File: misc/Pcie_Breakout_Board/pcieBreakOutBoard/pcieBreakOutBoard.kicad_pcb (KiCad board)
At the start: 2 copper layers, 53 x 45.2 mm, 1 part, among them J1 2041119-1 (Mini Pcie Express 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

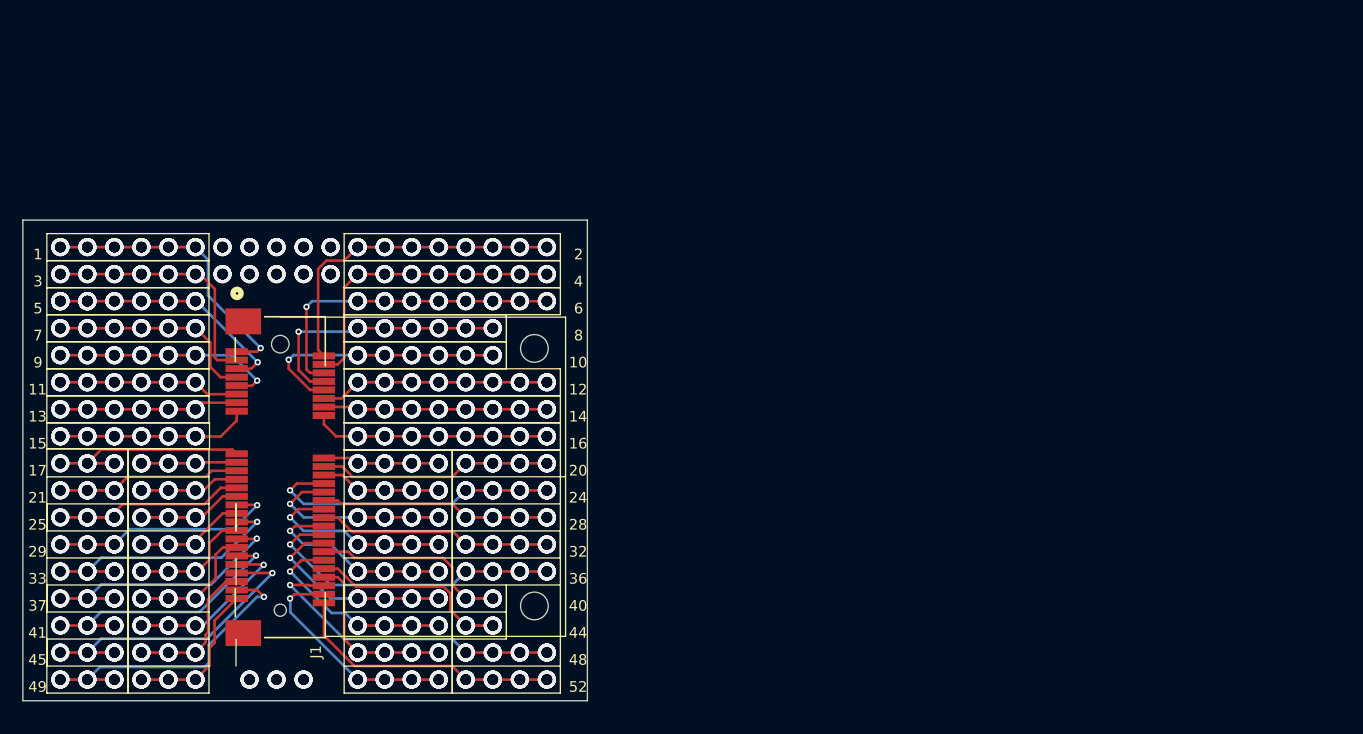
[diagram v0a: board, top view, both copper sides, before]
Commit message: routing
Start routing of the jtag part
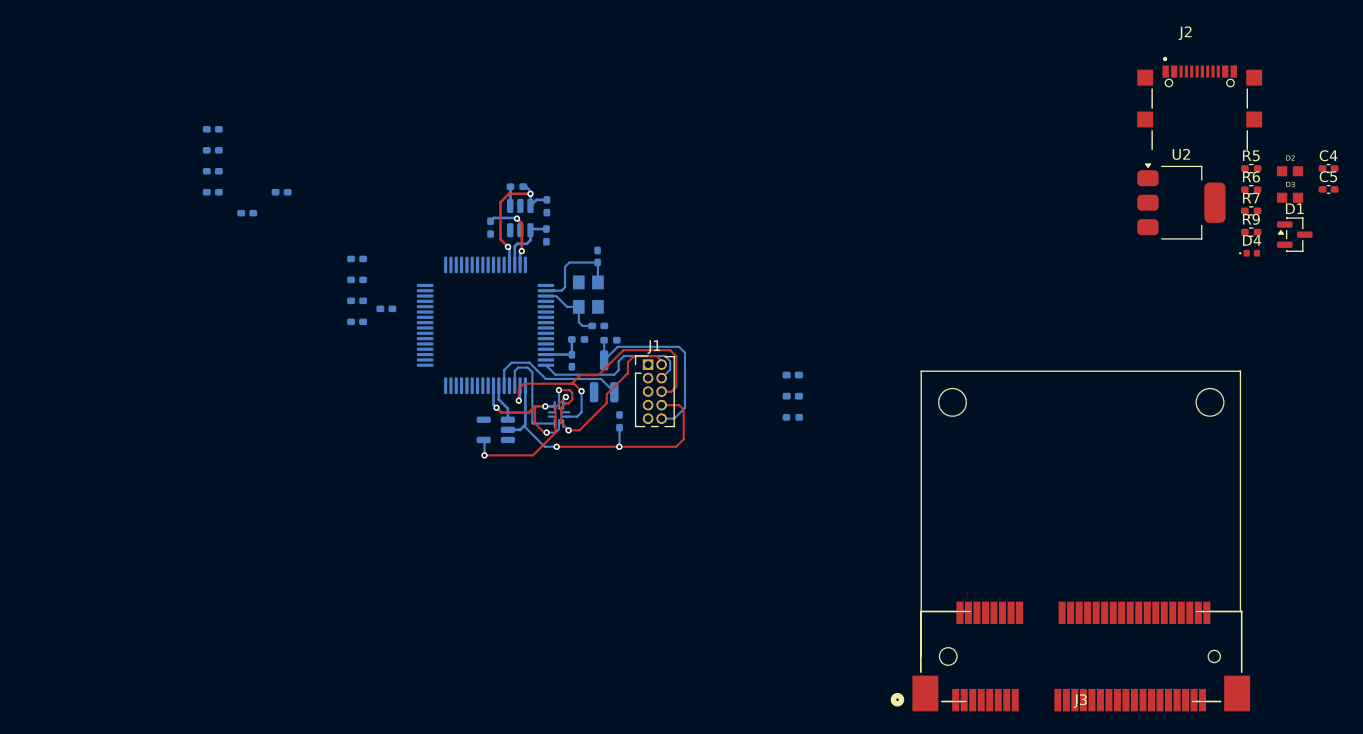
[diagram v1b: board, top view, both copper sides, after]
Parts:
- added C1: 27pF, Capacitor_SMD:C_0402_1005Metric_Pad0.74x0.62mm_HandSolder, B.Cu at (169.9, 81.1)
- added C10: 100nF, Capacitor_SMD:C_0402_1005Metric_Pad0.74x0.62mm_HandSolder, B.Cu at (147.3, 78.7)
- added C11: 3.3uF, Capacitor_SMD:C_0402_1005Metric_Pad0.74x0.62mm_HandSolder, B.Cu at (147.3, 80.7)
- added C12: 100nF, Capacitor_SMD:C_0402_1005Metric_Pad0.74x0.62mm_HandSolder, B.Cu at (136.9, 70.5)
- added C13: 100nF, Capacitor_SMD:C_0402_1005Metric_Pad0.74x0.62mm_HandSolder, B.Cu at (133.7, 62.6)
- added C15: 100nF, Capacitor_SMD:C_0402_1005Metric_Pad0.74x0.62mm_HandSolder, B.Cu at (133.7, 64.6)
- added C16: 100nF, Capacitor_SMD:C_0402_1005Metric_Pad0.74x0.62mm_HandSolder, B.Cu at (133.7, 66.5)
- added C17: 100nF, Capacitor_SMD:C_0402_1005Metric_Pad0.74x0.62mm_HandSolder, B.Cu at (133.7, 68.5)
- added C2: 10nF, Capacitor_SMD:C_0402_1005Metric_Pad0.74x0.62mm_HandSolder, B.Cu at (167.4, 84.3)
- added C3: 27pF, Capacitor_SMD:C_0402_1005Metric_Pad0.74x0.62mm_HandSolder, B.Cu at (169.9, 74.5)
- added C4: 1uF, Capacitor_SMD:C_0402_1005Metric_Pad0.74x0.62mm_HandSolder, F.Cu at (238.6, 66.3)
- added C5: 4.7uF, Capacitor_SMD:C_0402_1005Metric_Pad0.74x0.62mm_HandSolder, F.Cu at (238.6, 68.2)
- added C6: 100nF, Capacitor_SMD:C_0402_1005Metric_Pad0.74x0.62mm_HandSolder, B.Cu at (140.2, 68.5)
- added C7: 100nF, Capacitor_SMD:C_0402_1005Metric_Pad0.74x0.62mm_HandSolder, B.Cu at (150.0, 79.5)
- added C8: 4.1uF, Capacitor_SMD:C_0402_1005Metric_Pad0.74x0.62mm_HandSolder, B.Cu at (147.3, 74.8)
- added C9: 4.1uF, Capacitor_SMD:C_0402_1005Metric_Pad0.74x0.62mm_HandSolder, B.Cu at (147.3, 76.7)
- added D1: BAT54C, Package_TO_SOT_SMD:SOT-23, F.Cu at (235.4, 72.5)
- added D2: PGB1010603NR, User_Footprint:DIOC1608X36N, F.Cu at (234.9, 66.5)
- added D3: PGB1010603NR, User_Footprint:DIOC1608X36N, F.Cu at (234.9, 69.0)
- added D4: LED, LED_SMD:LED_0402_1005Metric, F.Cu at (231.3, 74.2)
- added J2: USB_C_Receptacle_USB2.0_16P, User_Footprint:AMPHENOL_GSB1C41110SSHR, F.Cu at (226.5, 60.8)
- added J3: 2041119-1 (Mini Pcie Express Half), User_Footprint:CONN_2041119-1_TEC, F.Cu at (215.3, 112.1)
- added L1: L, Inductor_SMD:L_0402_1005Metric_Pad0.77x0.64mm_HandSolder, B.Cu at (188.2, 85.7)
- added L2: L, Inductor_SMD:L_0402_1005Metric_Pad0.77x0.64mm_HandSolder, B.Cu at (188.2, 87.7)
- added Q1: MMBT2222A, Package_TO_SOT_SMD:SOT-23_Handsoldering, B.Cu at (170.5, 85.8)
- added R1: 12k, Resistor_SMD:R_0402_1005Metric_Pad0.72x0.64mm_HandSolder, B.Cu at (188.2, 89.7)
- added R10: 10k, Resistor_SMD:R_0402_1005Metric_Pad0.72x0.64mm_HandSolder, B.Cu at (165.1, 69.8)
- added R11: 10k, Resistor_SMD:R_0402_1005Metric_Pad0.72x0.64mm_HandSolder, B.Cu at (171.1, 82.4)
- added R12: 30K, Resistor_SMD:R_0402_1005Metric_Pad0.72x0.64mm_HandSolder, B.Cu at (171.9, 90.0)
- added R2: 10k, Resistor_SMD:R_0402_1005Metric_Pad0.72x0.64mm_HandSolder, B.Cu at (168.0, 82.3)
- added R3: 2k, Resistor_SMD:R_0402_1005Metric_Pad0.72x0.64mm_HandSolder, B.Cu at (162.3, 68.0)
- added R4: 10k, Resistor_SMD:R_0402_1005Metric_Pad0.72x0.64mm_HandSolder, B.Cu at (159.8, 71.8)
- added R5: 0, Resistor_SMD:R_0402_1005Metric_Pad0.72x0.64mm_HandSolder, F.Cu at (231.3, 66.3)
- added R6: 0, Resistor_SMD:R_0402_1005Metric_Pad0.72x0.64mm_HandSolder, F.Cu at (231.3, 68.3)
- added R7: 0, Resistor_SMD:R_0402_1005Metric_Pad0.72x0.64mm_HandSolder, F.Cu at (231.3, 70.3)
- added R8: 10k, Resistor_SMD:R_0402_1005Metric_Pad0.72x0.64mm_HandSolder, B.Cu at (165.1, 72.6)
- added R9: 100, Resistor_SMD:R_0402_1005Metric_Pad0.72x0.64mm_HandSolder, F.Cu at (231.3, 72.2)
- added U1: FT2232HL, Package_QFP:LQFP-64_10x10mm_P0.5mm, B.Cu at (159.3, 81.0)
- added U2: AP7361C-33E, Package_TO_SOT_SMD:SOT-223-3_TabPin2, F.Cu at (224.7, 69.5)
- added U3: 93LCxxBxxOT, Package_TO_SOT_SMD:SOT-23-6, B.Cu at (162.6, 70.9)
- added U4: NC7SZ125M5X, Package_TO_SOT_SMD:SOT-23-5, B.Cu at (160.3, 90.8)
- added U7: TS3A5223RSW, Package_DFN_QFN:Texas_RSW0010A_UQFN-10_1.4x1.8mm_P0.4mm, B.Cu at (166.2, 89.4)
- added Y1: ECS-120-20-33-AEL-TR, User_Footprint:XTAL_ECS-120-20-33-AEL-TR, B.Cu at (169.0, 78.1)
- J1: value 2041119-1 (Mini Pcie Express Half) -> Conn_ARM_JTAG_SWD_10; footprint User_Footprint:CONN_2041119-1_TEC -> Connector_PinHeader_1.27mm:PinHeader_2x05_P1.27mm_Vertical
- moved J1 36.1 mm to (174.6, 84.7), turned to 0 degrees
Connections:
- J1 pad 1: /Port1 -> +3V3
- J1 pad 10: /Port10 -> /Jtag/~{SRST}
- J1 pad 2: /Port2 -> /Jtag/TMS/SWDIO
- J1 pad 3: /Port3 -> GND
- J1 pad 4: /Port4 -> /Jtag/TCK/SWDCLK
- J1 pad 5: /Port5 -> GND
- J1 pad 6: /Port6 -> /Jtag/TDO
- J1 pad 7: /Port7 -> unconnected-(J1-KEY-Pad7)
- J1 pad 8: /Port8 -> /Jtag/TDI
- J1 pad 9: /Port9 -> GND
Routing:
- net /Port2: track 30.7 -> 0.00 mm, vias 24 -> 0
- net /Port6: track 30.5 -> 0.00 mm, vias 25 -> 0
- net /Port48: track 30.0 -> 0.00 mm, vias 13 -> 0
- net /Port36: track 29.8 -> 0.00 mm, vias 13 -> 0
- net /Port45: track 28.9 -> 0.00 mm, vias 9 -> 0
- net /Port49: track 28.7 -> 0.00 mm, vias 10 -> 0
- net /Port24: track 28.6 -> 0.00 mm, vias 13 -> 0
- net /Jtag/TDI: track 0.00 -> 28.5 mm, vias 0 -> 2
- net /Jtag/TDO: track 0.00 -> 28.4 mm, vias 0 -> 2
- net /Port4: track 28.3 -> 0.00 mm, vias 24 -> 0
- net /Port1: track 27.1 -> 0.00 mm, vias 19 -> 0
- net /Port52: track 25.7 -> 0.00 mm, vias 12 -> 0
- net /Port41: track 25.5 -> 0.00 mm, vias 9 -> 0
- net /Port37: track 25.3 -> 0.00 mm, vias 9 -> 0
- net /Port33: track 24.9 -> 0.00 mm, vias 9 -> 0
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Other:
- board size 53 x 45.2 mm -> 26.8 x 2.6 mm
- copper layers 2 -> 4
- board text removed: "1"
- board text removed: "10"
- board text removed: "11"
- board text removed: "12"
- board text removed: "13"
- board text removed: "14"
- board text removed: "15"
- board text removed: "16"
- board text removed: "17"
- board text removed: "18"
- board text removed: "19"
- board text removed: "2"
- board text removed: "20"
- board text removed: "21"
- board text removed: "22"
- board text removed: "23"
- board text removed: "24"
- board text removed: "25"
- board text removed: "26"
- board text removed: "27"
- board text removed: "28"
- board text removed: "29"
- board text removed: "3"
- board text removed: "30"
- board text removed: "31"
- board text removed: "32"
- board text removed: "33"
- board text removed: "34"
- board text removed: "35"
- board text removed: "36"
- board text removed: "37"
- board text removed: "38"
- board text removed: "39"
- board text removed: "4"
- board text removed: "40"
- board text removed: "41"
- board text removed: "42"
- board text removed: "43"
- board text removed: "44"
- board text removed: "45"
- board text removed: "46"
- board text removed: "47"
- board text removed: "48"
- board text removed: "49"
- board text removed: "5"
- board text removed: "50"
- board text removed: "51"
- board text removed: "52"
- board text removed: "6"
- board text removed: "7"
- board text removed: "8"
- board text removed: "9"

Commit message: layout
finished 70% of layout
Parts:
- added J4: Conn_02x04_Odd_Even, Connector_PinHeader_2.54mm:PinHeader_2x04_P2.54mm_Vertical, F.Cu at (136.6, 83.3)
- C13, C17, R1: moved to F.Cu
- C4, C5, D1, D2, D3, D4, R5, R6, R7, R9, U2: moved to B.Cu
- J3: footprint User_Footprint:CONN_2041119-1_TEC -> Connector_PCBEdge:BUS_PCI_Express_Mini_Half
- moved C4 108.8 mm to (130.3, 77.8), turned to 90 degrees
- moved C5 108.4 mm to (130.3, 74.2), turned to -90 degrees
- moved D1 107.6 mm to (127.8, 75.7), turned to -90 degrees
- moved D4 103.1 mm to (128.3, 70.7), turned to 180 degrees
- moved R9 102.9 mm to (128.4, 73.2)
- moved D3 102.7 mm to (132.3, 67.1), turned to 90 degrees
- moved R5 101.7 mm to (129.8, 72.2), turned to 180 degrees
- moved D2 100.5 mm to (134.4, 67.1), turned to -90 degrees
- moved R6 99.0 mm to (132.3, 70.8), turned to -90 degrees
- moved R7 97.0 mm to (134.3, 70.8), turned to -90 degrees
- moved J2 93.7 mm to (133.1, 68.6), turned to 180 degrees
- moved U2 89.2 mm to (135.8, 76.0)
- moved J3 60.8 mm to (155.9, 99.1)
- moved C13 35.0 mm to (162.3, 82.8)
- moved C15 34.0 mm to (158.0, 88.4)
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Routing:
- net /MiniPcieExHalf/Port8: track 0.00 -> 38.6 mm, vias 0 -> 3
- net /MiniPcieExHalf/Port4: track 0.00 -> 36.0 mm, vias 0 -> 2
- net /MiniPcieExHalf/Port12: track 0.00 -> 33.8 mm, vias 0 -> 3
- net /MiniPcieExHalf/Port18: track 0.00 -> 33.1 mm, vias 0 -> 1
- net /MiniPcieExHalf/Port6: track 0.00 -> 32.3 mm, vias 0 -> 3
- net /MiniPcieExHalf/Port20: track 0.00 -> 31.7 mm, vias 0 -> 1
- net /MiniPcieExHalf/Port16: track 0.00 -> 31.7 mm, vias 0 -> 3
- net /MiniPcieExHalf/Port2: track 0.00 -> 30.5 mm, vias 0 -> 2
- net /MiniPcieExHalf/Port22: track 0.00 -> 29.4 mm, vias 0 -> 1
- net /Jtag/~{DCD}: track 0.00 -> 27.8 mm, vias 0 -> 1
- net /MiniPcieExHalf/Port10: track 0.00 -> 27.3 mm, vias 0 -> 2
- net /MiniPcieExHalf/Port14: track 0.00 -> 26.7 mm, vias 0 -> 3
- net /Jtag/~{DSR}: track 0.00 -> 24.6 mm, vias 0 -> 1
- net /Jtag/TXD: track 0.00 -> 23.4 mm, vias 0 -> 1
- net /Jtag/RXD: track 0.00 -> 21.9 mm, vias 0 -> 1
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- added copper zone on In2.Cu, net +3V3
- added copper zone on In1.Cu, net GND
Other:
- board size 26.8 x 2.6 mm -> 54 x 50.8 mm

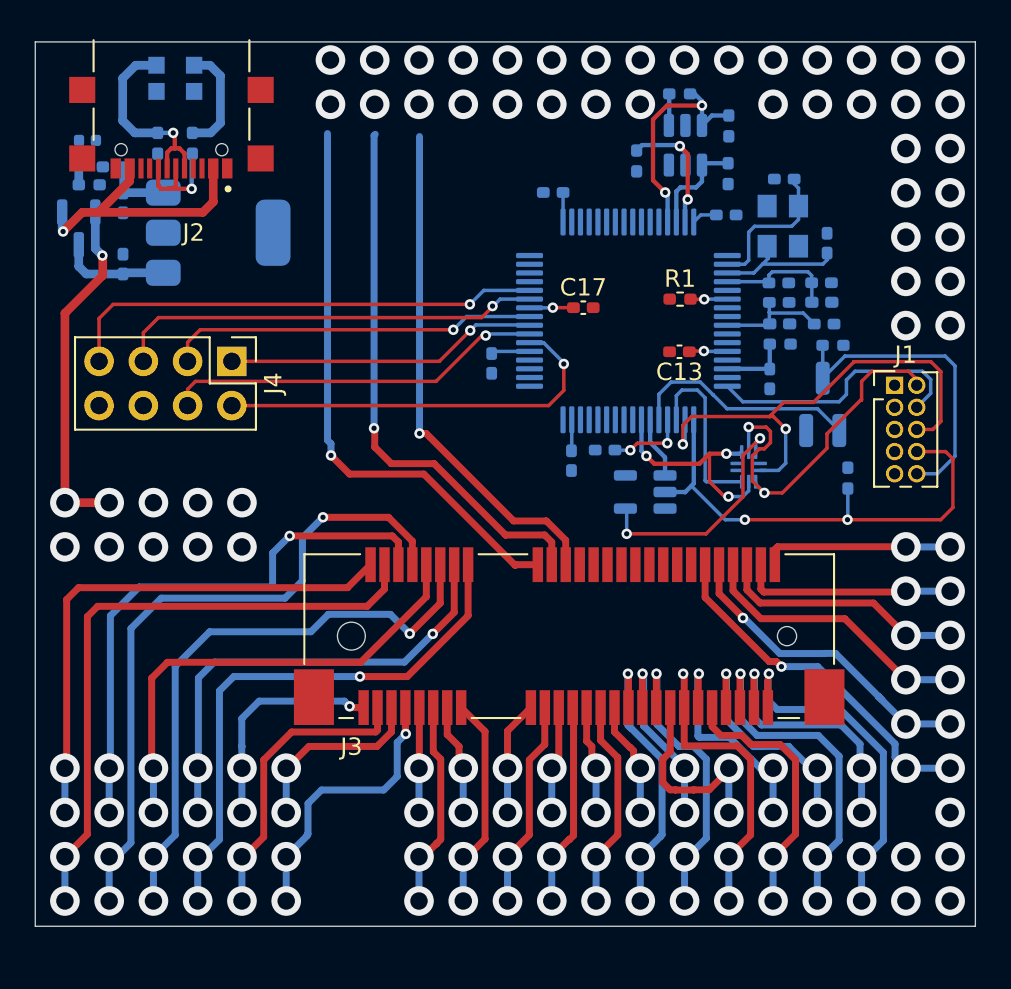
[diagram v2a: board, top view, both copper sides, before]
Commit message: Routing
Finish layout needs to be checked
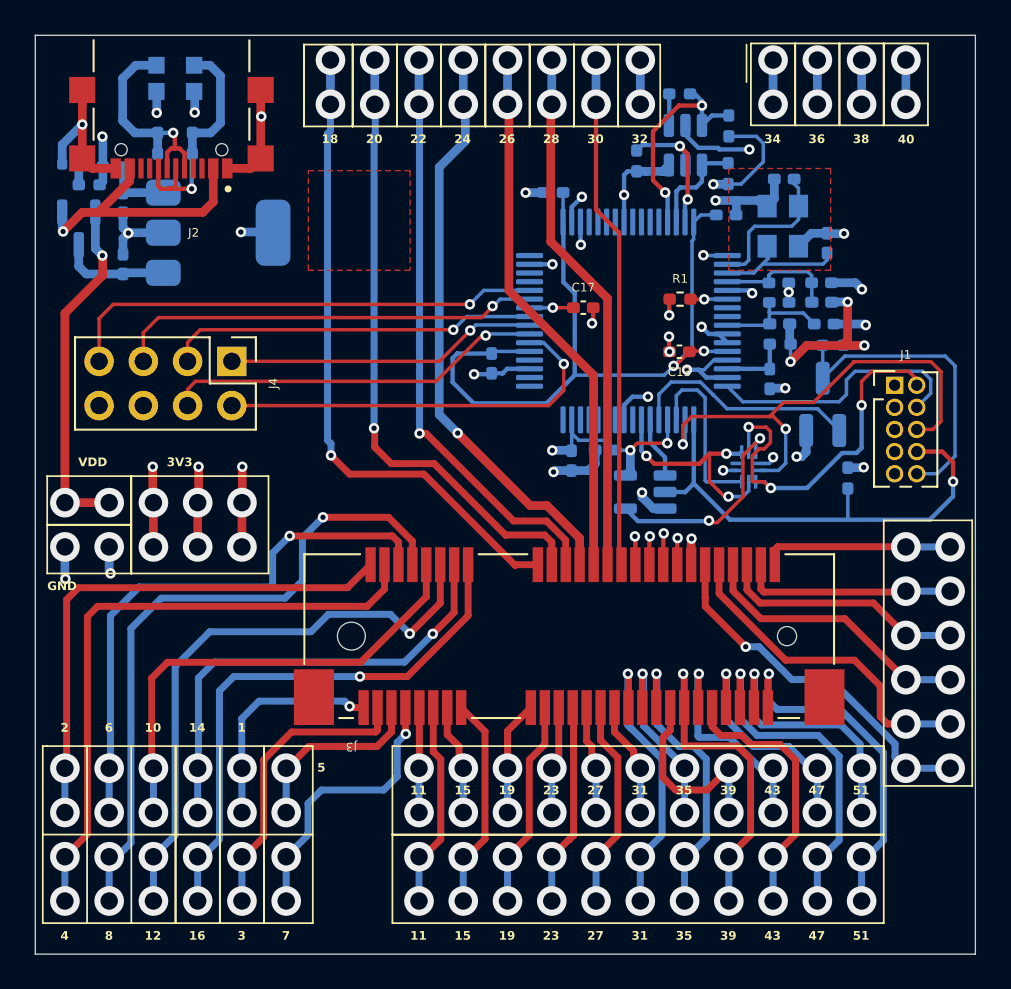
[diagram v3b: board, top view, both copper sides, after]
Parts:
- moved D4 1.67 mm to (127.3, 72.0), turned to 0 degrees
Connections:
- net /Power3v3/DM renamed /Power/DM
- net /Power3v3/DP renamed /Power/DP
- net /Power3v3/VDD renamed /Power/VDD
- net /Power3v3/Vbus renamed /Power/Vbus
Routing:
- net GND: track 0.00 -> 78.9 mm, vias 2 -> 34
- net +3V3: track 8.83 -> 59.0 mm, vias 9 -> 22
- net +1V8: track 7.58 -> 44.2 mm, vias 1 -> 2
- net /MiniPcieExHalf/Port40: track 0.00 -> 35.9 mm, vias 0 -> 3
- net /MiniPcieExHalf/Port38: track 0.00 -> 33.7 mm, vias 0 -> 3
- net /MiniPcieExHalf/Port24: track 0.00 -> 33.5 mm, vias 0 -> 3
- net /MiniPcieExHalf/Port36: track 0.00 -> 32.7 mm, vias 0 -> 3
- net /MiniPcieExHalf/Port34: track 0.00 -> 31.9 mm, vias 0 -> 3
- net /MiniPcieExHalf/Port26: track 0.00 -> 31.0 mm, vias 0 -> 2
- net /MiniPcieExHalf/Port28: track 0.00 -> 30.3 mm, vias 0 -> 2
- net /MiniPcieExHalf/Port32: track 0.00 -> 29.9 mm, vias 0 -> 3
- net /MiniPcieExHalf/Port30: track 0.00 -> 29.4 mm, vias 0 -> 2
- net /MiniPcieExHalf/Port22: track 29.4 -> 33.8 mm, vias 1 -> 3
- net /MiniPcieExHalf/Port18: track 33.1 -> 37.3 mm, vias 1 -> 3
- net /MiniPcieExHalf/Port20: track 31.7 -> 36.0 mm, vias 1 -> 3
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- added copper zone on F.Cu, net (none)
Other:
- board size 54 x 50.8 mm -> 54 x 52.7 mm
- board text added: "1"
- board text added: "10"
- board text added: "11"
- board text added: "12"
- board text added: "14"
- board text added: "15"
- board text added: "16"
- board text added: "18"
- board text added: "19"
- board text added: "2"
- board text added: "20"
- board text added: "22"
- board text added: "23"
- board text added: "24"
- board text added: "26"
- board text added: "27"
- board text added: "28"
- board text added: "3"
- board text added: "30"
- board text added: "31"
- board text added: "32"
- board text added: "34"
- board text added: "35"
- board text added: "36"
- board text added: "38"
- board text added: "39"
- board text added: "3V3"
- board text added: "4"
- board text added: "40"
- board text added: "43"
- board text added: "47"
- board text added: "5"
- board text added: "51"
- board text added: "6"
- board text added: "7"
- board text added: "8"
- board text added: "GND"
- board text added: "VDD"
